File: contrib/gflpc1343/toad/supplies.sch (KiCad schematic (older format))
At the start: 84 parts, among them Q1 MOSFET_P, U17 MC4558, U18 GSG-MC34063, U19 MC4558, U20 GSG-MC34063, U21 BH2228FV, U22 MC4558, U23 DG409, U24 DG409, U25 DG409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

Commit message: TOAD: power indicator LED, some component selection
git-svn-id: https://svn.code.sf.net/p/goodfet/code@1623 12e2690d-a6be-4b82-a7b7-67c4a43b65c8
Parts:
- added D3: PWRLED, symbol LED
- added R90: 470, symbol R
- C25, C31, C34, C38: Description (none) -> CAP ALUM 100UF 35V 20% SMD; Manufacturer (none) -> Nichicon; Part Number (none) -> UWT1V101MCL1GS
- U18, U20: Description (none) -> IC REG BUCK BOOST INV ADJ 8SOIC; Manufacturer (none) -> STMicroelectronics; Part Number (none) -> MC34063ACD-TR
- U23, U24, U25: Description (none) -> IC MUX CMOS ANG DUAL 8CH 16TSSOP; Manufacturer (none) -> Vishay Siliconix; Part Number (none) -> DG409LDQ-T1-E3
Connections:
- net !VEN: now also D3.2 (K)
- net 3V3: now also R90.2
- new net: D3.1 (A), R90.1

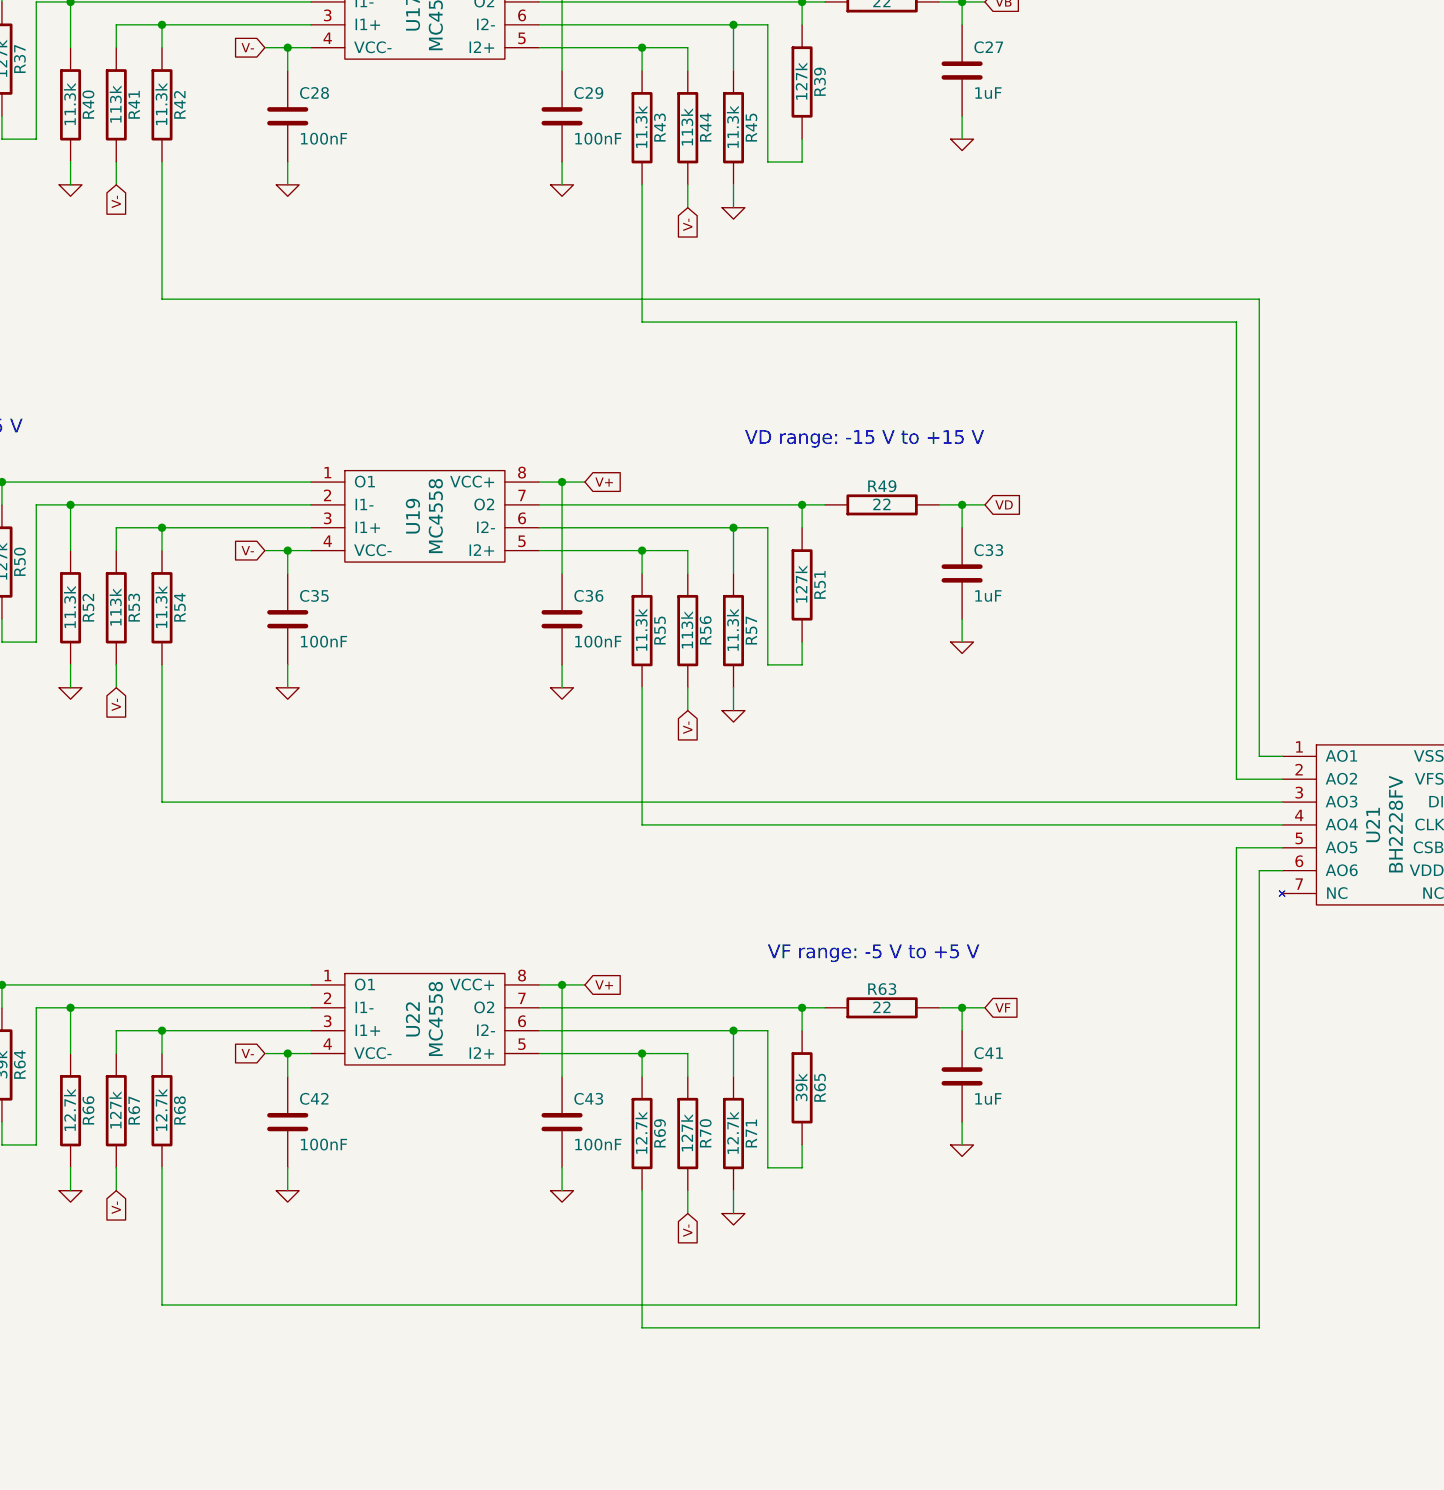
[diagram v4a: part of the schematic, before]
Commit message: completed TOAD design
git-svn-id: https://svn.code.sf.net/p/goodfet/code@1656 12e2690d-a6be-4b82-a7b7-67c4a43b65c8
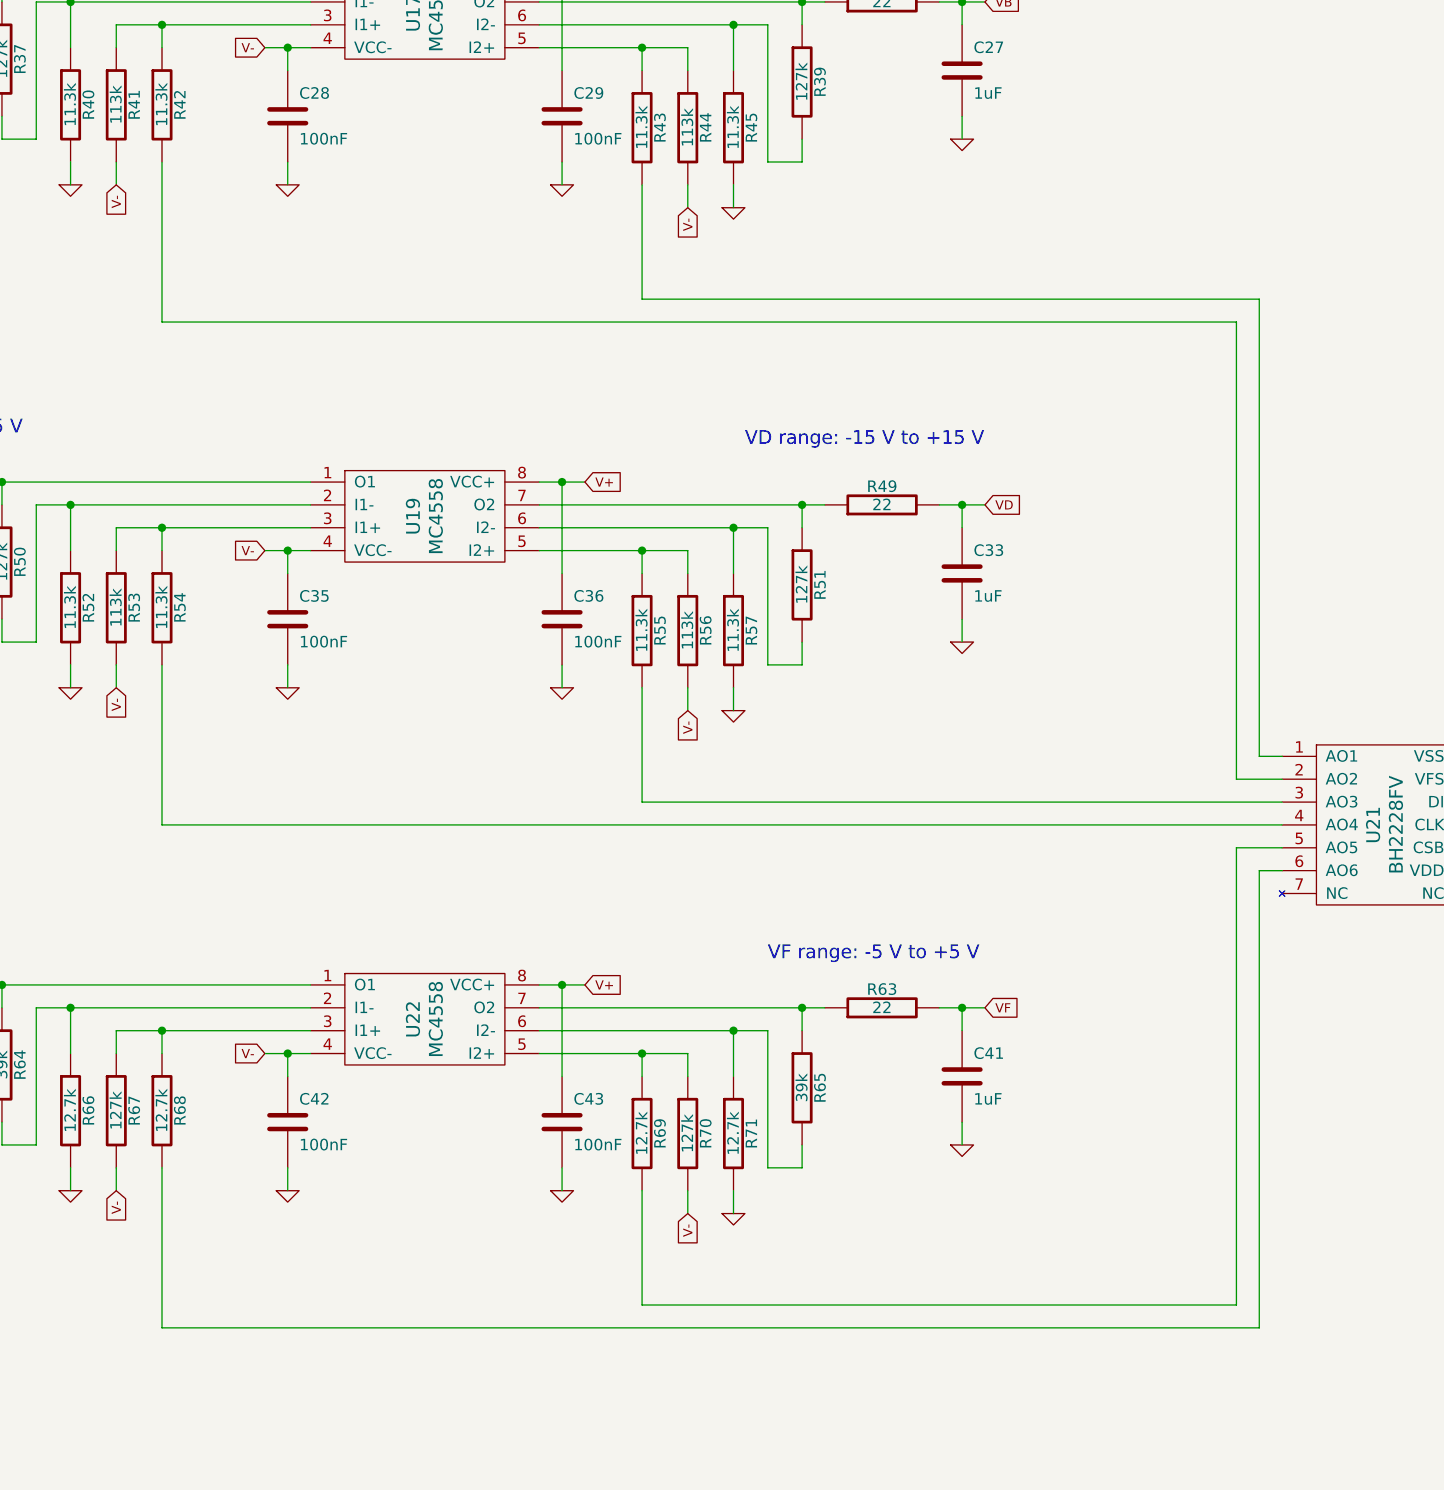
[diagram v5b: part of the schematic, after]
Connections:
- net at U21.1 (AO1): now also R43.2; no longer R42.2
- net at U21.2 (AO2): now also R42.2; no longer R43.2
- net at U21.3 (AO3): now also R55.2; no longer R54.2
- net at U21.4 (AO4): now also R54.2; no longer R55.2
- net at U21.5 (AO5): now also R69.2; no longer R68.2
- net at U21.6 (AO6): now also R68.2; no longer R69.2
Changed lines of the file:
@@
-EESchema Schematic File Version 2  date Thu Jul 18 17:37:42 2013
+EESchema Schematic File Version 2  date Mon Jul 22 09:26:32 2013
 LIBS:power
 LIBS:device
@@
 Sheet 3 4
 Title ""
-Date "18 jul 2013"
+Date "22 jul 2013"
 Rev ""
 Comp ""
@@
 Connection ~ 8900 1900
 Wire Wire Line
-	8900 2500 8900 3100
-Wire Wire Line
-	8900 3100 13700 3100
-Wire Wire Line
 	8700 2600 8700 2500
 Wire Wire Line
@@
 	11000 2000 11000 2100
 Wire Wire Line
-	11000 2600 11000 3200
-Wire Wire Line
-	11000 3200 13600 3200
-Wire Wire Line
 	11200 2600 11200 2700
 Wire Wire Line
@@
 Connection ~ 8900 4100
 Wire Wire Line
-	8900 4700 8900 5300
-Wire Wire Line
 	8700 4800 8700 4700
 Wire Wire Line
@@
 	11000 4200 11000 4300
 Wire Wire Line
-	11000 4800 11000 5400
-Wire Wire Line
 	11200 4800 11200 4900
 Wire Wire Line
@@
 Connection ~ 8900 6300
 Wire Wire Line
-	8900 6900 8900 7500
-Wire Wire Line
 	8700 7000 8700 6900
 Wire Wire Line
@@
 	11000 6400 11000 6500
 Wire Wire Line
-	11000 7000 11000 7600
-Wire Wire Line
 	11200 7000 11200 7100
 Wire Wire Line
@@
 Connection ~ 12400 6200
 Wire Wire Line
-	8900 5300 13800 5300
-Wire Wire Line
-	11000 5400 13800 5400
-Wire Wire Line
 	13800 5100 13700 5100
 Wire Wire Line
@@
 	13600 5200 13600 3200
 Wire Wire Line
-	11000 7600 13700 7600
-Wire Wire Line
 	13700 7600 13700 5600
 Wire Wire Line
@@
 Wire Wire Line
 	13600 5500 13600 7500
-Wire Wire Line
-	13600 7500 8900 7500
 Wire Wire Line
 	14800 5100 14700 5100
@@
 	1    0    0    -1
 $EndComp
+Wire Wire Line
+	13700 3100 11000 3100
+Wire Wire Line
+	11000 3100 11000 2600
+Wire Wire Line
+	13600 3200 8900 3200
+Wire Wire Line
+	8900 3200 8900 2500
+Wire Wire Line
+	13800 5300 11000 5300
+Wire Wire Line
+	11000 5300 11000 4800
+Wire Wire Line
+	8900 4700 8900 5400
+Wire Wire Line
+	8900 5400 13800 5400
+Wire Wire Line
+	13600 7500 11000 7500
+Wire Wire Line
+	11000 7500 11000 7000
+Wire Wire Line
+	13700 7600 8900 7600
+Wire Wire Line
+	8900 7600 8900 6900
 $EndSCHEMATC

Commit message: TOAD: fixed part numbers for DG408/DG409
git-svn-id: https://svn.code.sf.net/p/goodfet/code@1660 12e2690d-a6be-4b82-a7b7-67c4a43b65c8
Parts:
- U23, U24, U25: Part Number DG409LDQ-T1-E3 -> DG409DQ-T1-E3
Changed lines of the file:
@@
 F 1 "DG409" V 2050 7600 60  0000 C CNN
 F 4 "Vishay Siliconix" H 2100 7600 60  0001 C CNN "Manufacturer"
-F 5 "DG409LDQ-T1-E3" H 2100 7600 60  0001 C CNN "Part Number"
+F 5 "DG409DQ-T1-E3" H 2100 7600 60  0001 C CNN "Part Number"
 F 6 "IC MUX CMOS ANG DUAL 8CH 16TSSOP" H 2100 7600 60  0001 C CNN "Description"
 	1    2100 7600
@@
 F 1 "DG409" V 4650 7600 60  0000 C CNN
 F 4 "Vishay Siliconix" H 4700 7600 60  0001 C CNN "Manufacturer"
-F 5 "DG409LDQ-T1-E3" H 4700 7600 60  0001 C CNN "Part Number"
+F 5 "DG409DQ-T1-E3" H 4700 7600 60  0001 C CNN "Part Number"
 F 6 "IC MUX CMOS ANG DUAL 8CH 16TSSOP" H 4700 7600 60  0001 C CNN "Description"
 	1    4700 7600
@@
 F 1 "DG409" V 4650 9000 60  0000 C CNN
 F 4 "Vishay Siliconix" H 4700 9000 60  0001 C CNN "Manufacturer"
-F 5 "DG409LDQ-T1-E3" H 4700 9000 60  0001 C CNN "Part Number"
+F 5 "DG409DQ-T1-E3" H 4700 9000 60  0001 C CNN "Part Number"
 F 6 "IC MUX CMOS ANG DUAL 8CH 16TSSOP" H 4700 9000 60  0001 C CNN "Description"
 	1    4700 9000

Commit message: Similar updates to those found in the layout for repairing V+/V-
git-svn-id: https://svn.code.sf.net/p/goodfet/code@1665 12e2690d-a6be-4b82-a7b7-67c4a43b65c8
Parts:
- C25, C31, C34, C38: symbol C -> CP1
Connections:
- net GND: now also C34.1; no longer C34.2
- net V-: now also C34.2; no longer C34.1
- net at R58.2, U20.7 (IPK), U20.8 (DRC): now also U20.1 (SWC)
- net at D2.2 (K): now also L2.2, U20.2 (SWE); no longer U20.1 (SWC)
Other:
- moved on the sheet: L2
